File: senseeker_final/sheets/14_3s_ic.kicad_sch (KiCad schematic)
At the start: 40 parts, among them P11 1.27mm/1*3p, Q10 AO3400A, Q11 AO3401A, Q9 AO3400A, U12 BQ24170RGYR, U16 NTC10K/0805/F

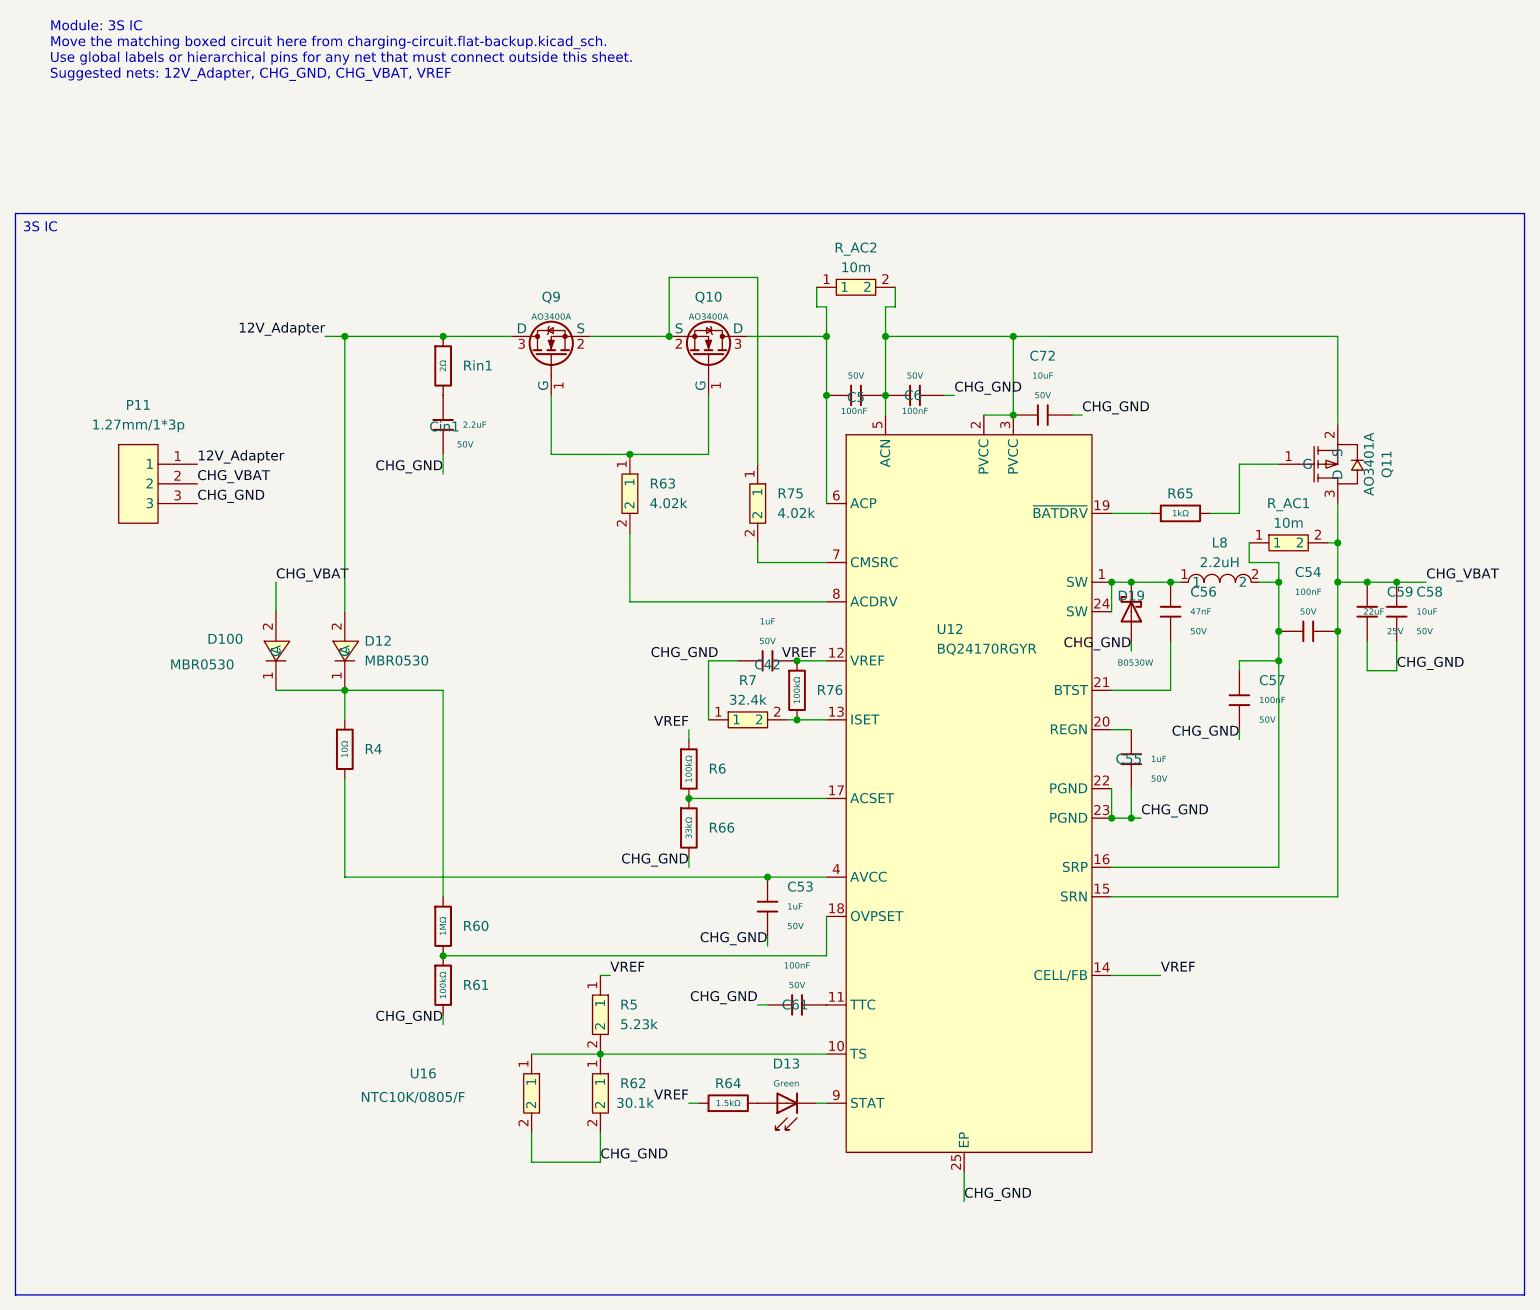
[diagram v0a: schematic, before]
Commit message: formatting changes for LM2596, now ready to branch of off and make our seperate PCB and then compare
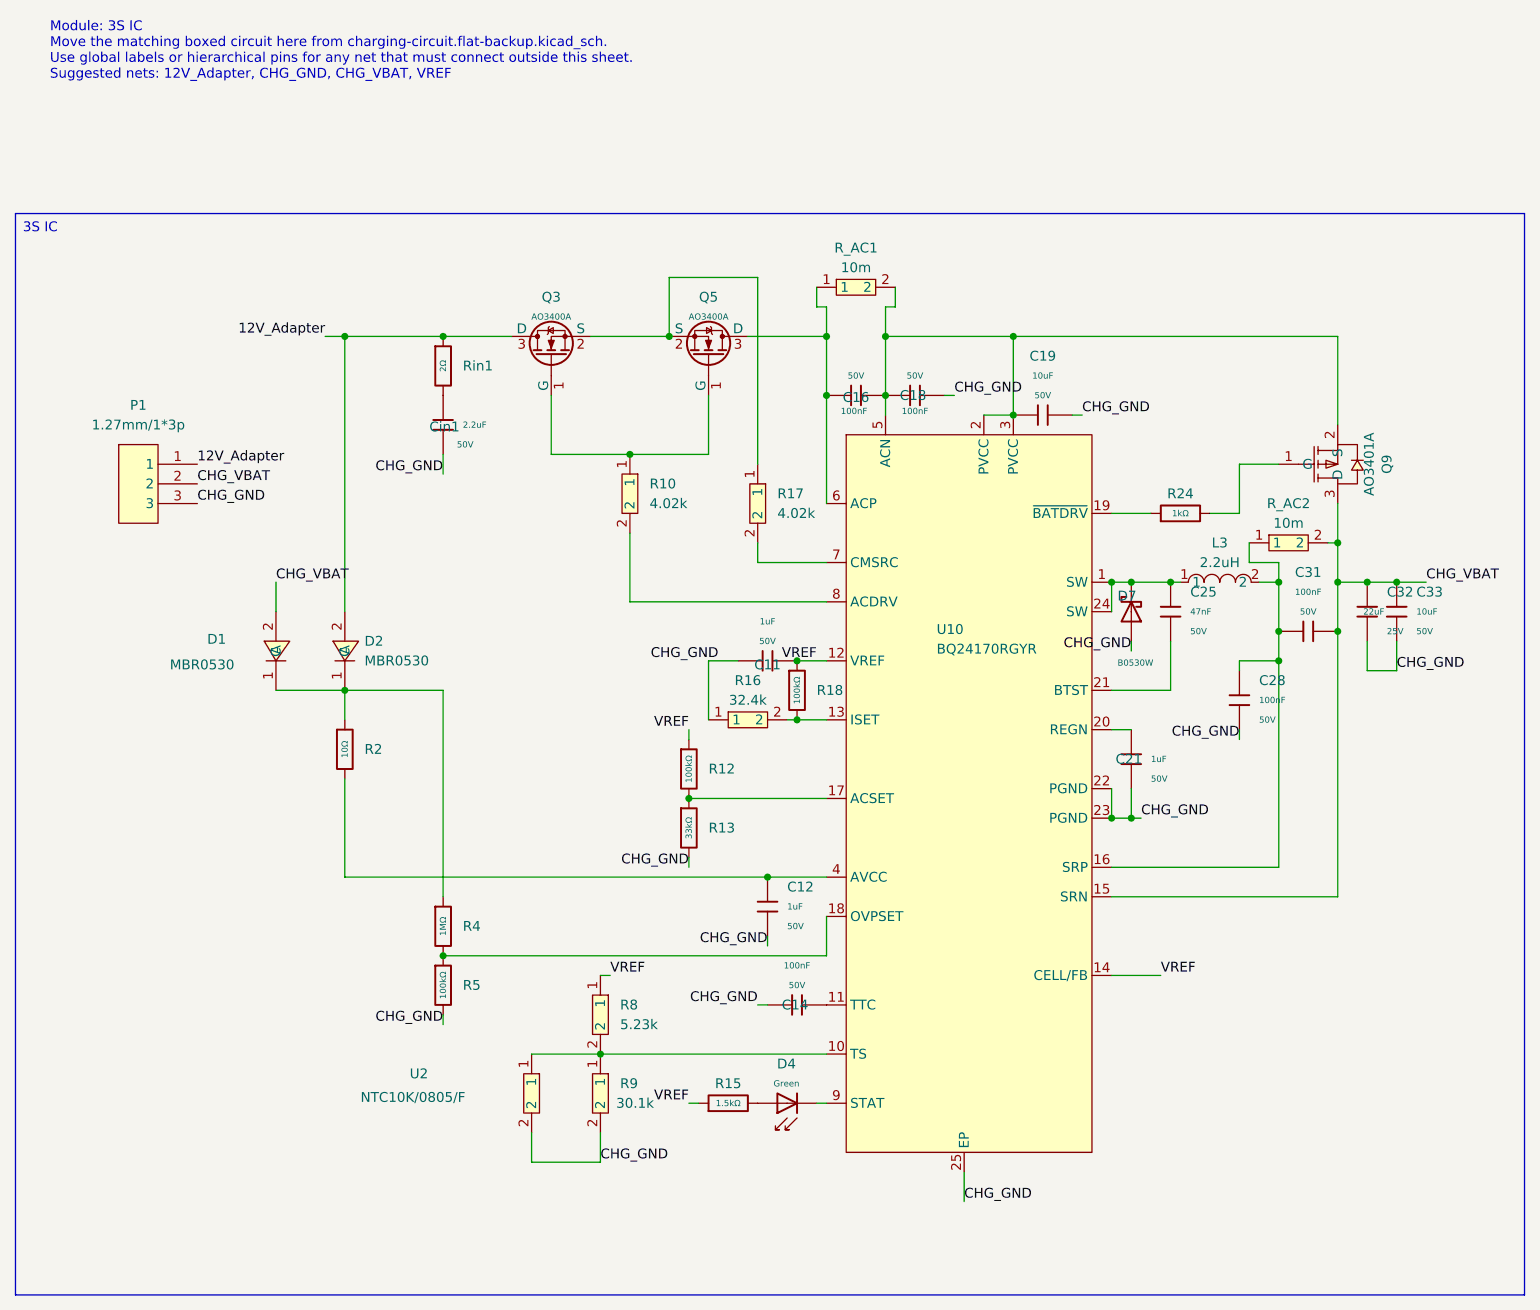
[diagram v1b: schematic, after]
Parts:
- renumbered C42 to C11, C53 to C12, C61 to C14, C5 to C16, C6 to C18, C72 to C19, C55 to C21, C56 to C25, C57 to C28, C54 to C31, C59 to C32, C58 to C33, D100 to D1, D12 to D2, D13 to D4, D19 to D7, L8 to L3, P11 to P1, Q9 to Q3, Q10 to Q5, Q11 to Q9, R63 to R10, R6 to R12, R66 to R13, R64 to R15, R7 to R16, R75 to R17, R76 to R18, R4 to R2, R65 to R24, R60 to R4, R61 to R5, R5 to R8, R62 to R9, R_AC2 to R_AC1, R_AC1 to R_AC2, U12 to U10, U16 to U2
